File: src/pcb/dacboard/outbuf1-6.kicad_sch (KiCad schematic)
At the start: 18 parts, among them U59 AD8675ARZ, U60 AD8675ARZ, U61 AD8675ARZ, U62 AD8675ARZ, U63 AD8675ARZ, U64 AD8675ARZ

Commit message: dacboard routing
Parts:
- C47, C48, C49, C50, C51, C52: footprint (none) -> Capacitor_SMD:C_0603_1608Metric_Pad1.08x0.95mm_HandSolder
- R16, R17, R18, R19, R20, R21: footprint (none) -> Resistor_SMD:R_0805_2012Metric
- U59, U60, U61, U62, U63, U64: footprint R_8_ADI -> Package_SO:SOIC-8_3.9x4.9mm_P1.27mm
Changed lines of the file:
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@@
 			)
 		)
-		(property "Footprint" ""
+		(property "Footprint" "Capacitor_SMD:C_0603_1608Metric_Pad1.08x0.95mm_HandSolder"
 			(at 166.0652 54.61 0)
 			(effects
@@
 			)
 		)
-		(property "Footprint" ""
+		(property "Footprint" "Capacitor_SMD:C_0603_1608Metric_Pad1.08x0.95mm_HandSolder"
 			(at 166.0652 130.81 0)
 			(effects
@@
 			)
 		)
-		(property "Footprint" ""
+		(property "Footprint" "Resistor_SMD:R_0805_2012Metric"
 			(at 258.064 124.714 90)
 			(effects
@@
 			)
 		)
-		(property "Footprint" ""
+		(property "Footprint" "Capacitor_SMD:C_0603_1608Metric_Pad1.08x0.95mm_HandSolder"
 			(at 166.0652 91.44 0)
 			(effects
@@
 			)
 		)
-		(property "Footprint" ""
+		(property "Footprint" "Capacitor_SMD:C_0603_1608Metric_Pad1.08x0.95mm_HandSolder"
 			(at 35.2552 133.35 0)
 			(effects
@@
 			)
 		)
-		(property "Footprint" "R_8_ADI"
+		(property "Footprint" "Package_SO:SOIC-8_3.9x4.9mm_P1.27mm"
 			(at 182.88 44.45 0)
 			(effects
@@
 			)
 		)
-		(property "Footprint" ""
+		(property "Footprint" "Resistor_SMD:R_0805_2012Metric"
 			(at 258.064 85.344 90)
 			(effects
@@
 			)
 		)
-		(property "Footprint" "R_8_ADI"
+		(property "Footprint" "Package_SO:SOIC-8_3.9x4.9mm_P1.27mm"
 			(at 182.88 120.65 0)
 			(effects
@@
 			)
 		)
-		(property "Footprint" ""
+		(property "Footprint" "Capacitor_SMD:C_0603_1608Metric_Pad1.08x0.95mm_HandSolder"
 			(at 35.2552 91.44 0)
 			(effects
@@
 			)
 		)
-		(property "Footprint" "R_8_ADI"
+		(property "Footprint" "Package_SO:SOIC-8_3.9x4.9mm_P1.27mm"
 			(at 182.88 81.28 0)
 			(effects
@@
 			)
 		)
-		(property "Footprint" ""
+		(property "Footprint" "Capacitor_SMD:C_0603_1608Metric_Pad1.08x0.95mm_HandSolder"
 			(at 35.2552 54.61 0)
 			(effects
@@
 			)
 		)
-		(property "Footprint" ""
+		(property "Footprint" "Resistor_SMD:R_0805_2012Metric"
 			(at 258.064 48.514 90)
 			(effects
@@
 			)
 		)
-		(property "Footprint" "R_8_ADI"
+		(property "Footprint" "Package_SO:SOIC-8_3.9x4.9mm_P1.27mm"
 			(at 52.07 81.28 0)
 			(effects
@@
 			)
 		)
-		(property "Footprint" ""
+		(property "Footprint" "Resistor_SMD:R_0805_2012Metric"
 			(at 127.254 85.344 90)
 			(effects
@@
 			)
 		)
-		(property "Footprint" "R_8_ADI"
+		(property "Footprint" "Package_SO:SOIC-8_3.9x4.9mm_P1.27mm"
 			(at 52.07 123.19 0)
 			(effects
@@
 			)
 		)
-		(property "Footprint" ""
+		(property "Footprint" "Resistor_SMD:R_0805_2012Metric"
 			(at 127.254 48.514 90)
 			(effects
@@
 			)
 		)
-		(property "Footprint" "R_8_ADI"
+		(property "Footprint" "Package_SO:SOIC-8_3.9x4.9mm_P1.27mm"
 			(at 52.07 44.45 0)
 			(effects
@@
 			)
 		)
-		(property "Footprint" ""
+		(property "Footprint" "Resistor_SMD:R_0805_2012Metric"
 			(at 127.254 127.254 90)
 			(effects

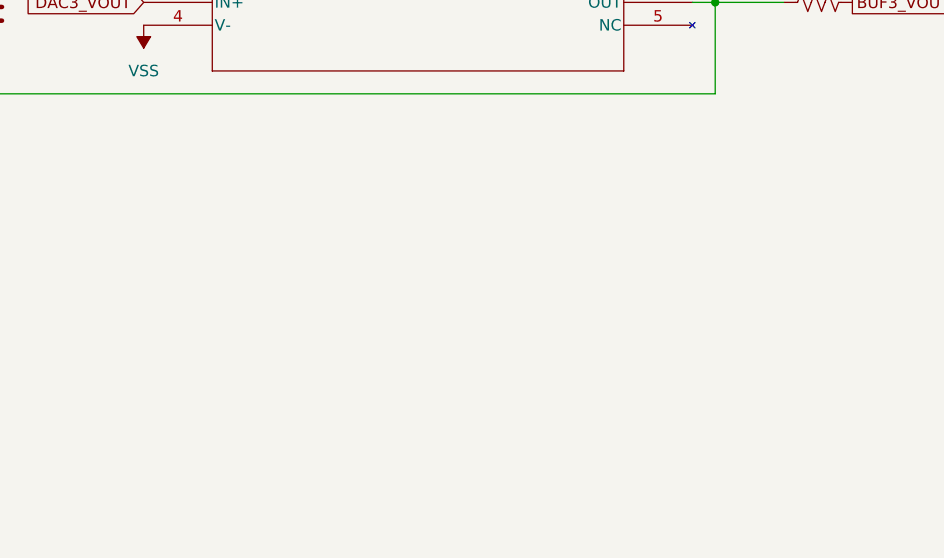
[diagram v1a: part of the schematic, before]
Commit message: got rid of all drc errors
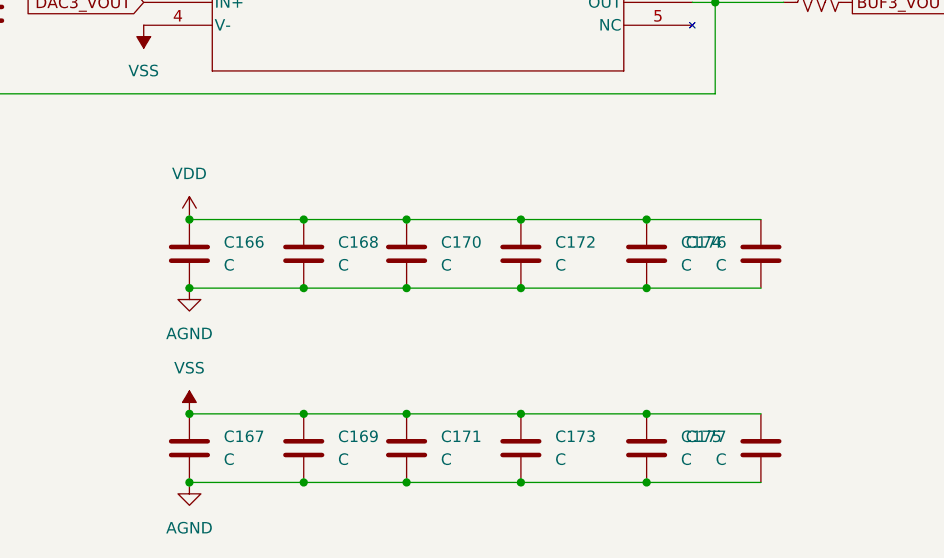
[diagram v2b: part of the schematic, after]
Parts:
- added C166, C167, C168, C169, C170, C171, C172, C173, C174, C175, C176, C177: C, Capacitor_SMD:C_0402_1005Metric_Pad0.74x0.62mm_HandSolder, symbol Device:C
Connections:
- net VDD: now also C166.1, C168.1, C170.1, C172.1, C174.1, C176.1
- net VSS: now also C167.1, C169.1, C171.1, C173.1, C175.1, C177.1
- new net AGND: C166.2, C167.2, C168.2, C169.2, C170.2, C171.2, C172.2, C173.2, C174.2, C175.2, C176.2, C177.2
